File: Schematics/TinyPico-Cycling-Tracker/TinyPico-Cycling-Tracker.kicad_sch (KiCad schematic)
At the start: 7 parts, among them SW1 SW_Push, U1 TinyPico, U2 module_mpu6050, U3 SSD1306 0.96" OLED, U4 GPS6MV2, U5 MicroSD Card Adapter

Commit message: fix: use 5V power pin only
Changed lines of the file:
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@@
-	)
-	(junction
-		(at 113.03 35.56)
-		(diameter 0)
-		(color 0 0 0 0)
 	)
 	(junction
@@
 	(wire
 		(pts
-			(xy 113.03 35.56) (xy 143.51 35.56)
+			(xy 91.44 35.56) (xy 143.51 35.56)
 		)
 		(stroke
@@
 	(wire
 		(pts
-			(xy 113.03 33.02) (xy 113.03 35.56)
-		)
-		(stroke
-			(width 0)
-			(type default)
-		)
-	)
-	(wire
-		(pts
 			(xy 110.49 57.15) (xy 120.65 57.15)
 		)
@@
 		(pts
 			(xy 147.32 43.18) (xy 168.91 43.18)
-		)
-		(stroke
-			(width 0)
-			(type default)
-		)
-	)
-	(wire
-		(pts
-			(xy 91.44 35.56) (xy 113.03 35.56)
 		)
 		(stroke
@@
 					(unit 1)
 				)
-			)
-		)
-	)
-	(symbol
-		(lib_id "power:PWR_FLAG")
-		(at 113.03 33.02 0)
-		(unit 1)
-		(exclude_from_sim no)
-		(in_bom yes)
-		(on_board yes)
-		(dnp no)
-		(fields_autoplaced yes)
-		(property "Reference" "#FLG01"
-			(at 113.03 31.115 0)
-			(effects
-				(font
-					(size 1.27 1.27)
-				)
-				(hide yes)
-			)
-		)
-		(property "Value" "PWR_FLAG"
-			(at 113.03 27.94 0)
-			(effects
-				(font
-					(size 1.27 1.27)
-				)
-			)
-		)
-		(property "Footprint" ""
-			(at 113.03 33.02 0)
-			(effects
-				(font
-					(size 1.27 1.27)
-				)
-				(hide yes)
-			)
-		)
-		(property "Datasheet" "~"
-			(at 113.03 33.02 0)
-			(effects
-				(font
-					(size 1.27 1.27)
-				)
-				(hide yes)
-			)
-		)
-		(property "Description" "Special symbol for telling ERC where power comes from"
-			(at 113.03 33.02 0)
-			(effects
-				(font
-					(size 1.27 1.27)
-				)
-				(hide yes)
-			)
-		)
-		(pin "1"
-		)
-		(instances
-			(project ""
-				(path "/c19b4b11-d562-4619-8198-7fbe4f513d32"
-					(reference "#FLG01")
-					(unit 1)
-				)

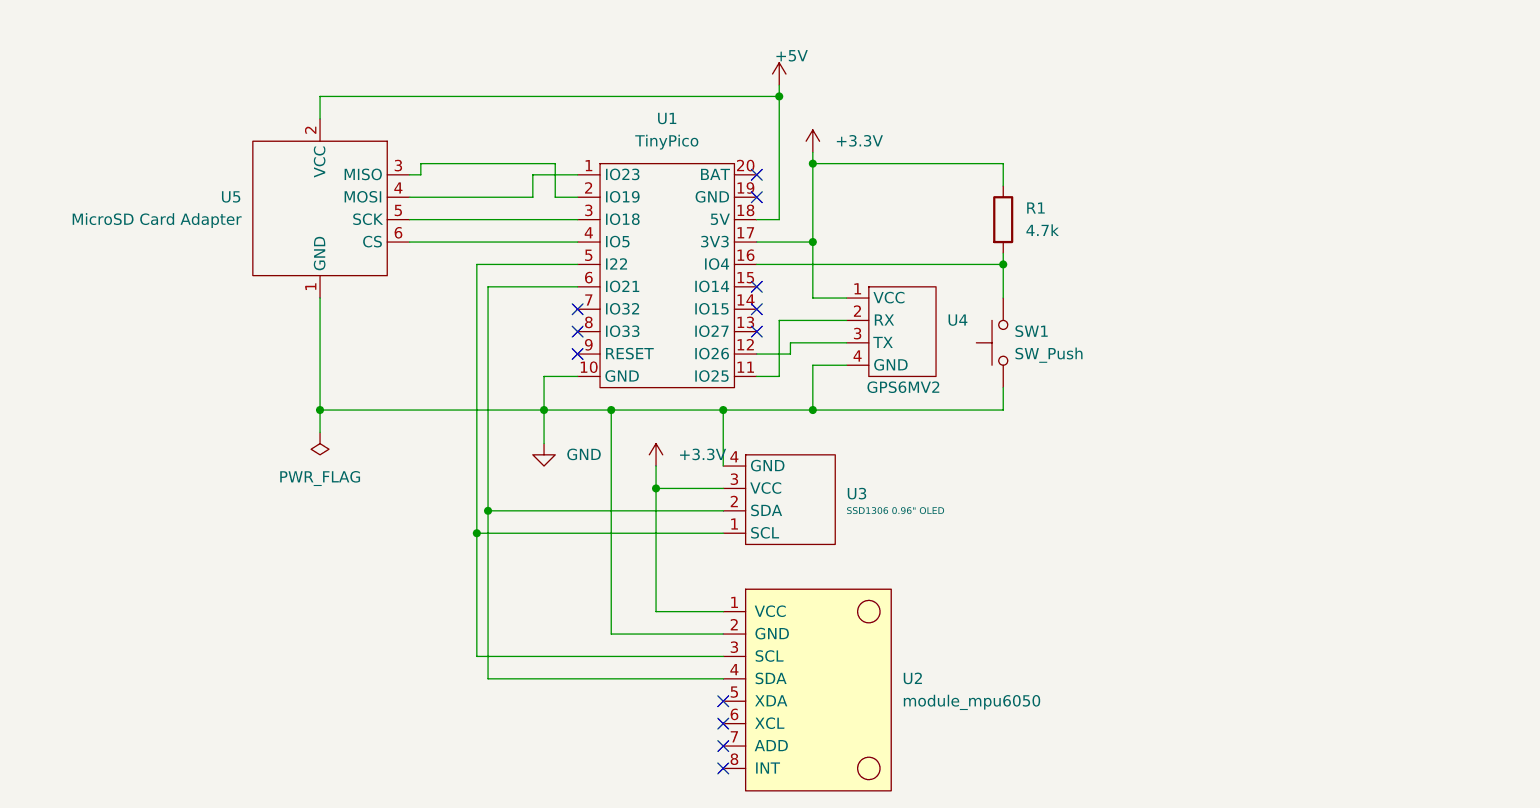
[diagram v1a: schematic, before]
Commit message: chore: use multisheet for the schematic
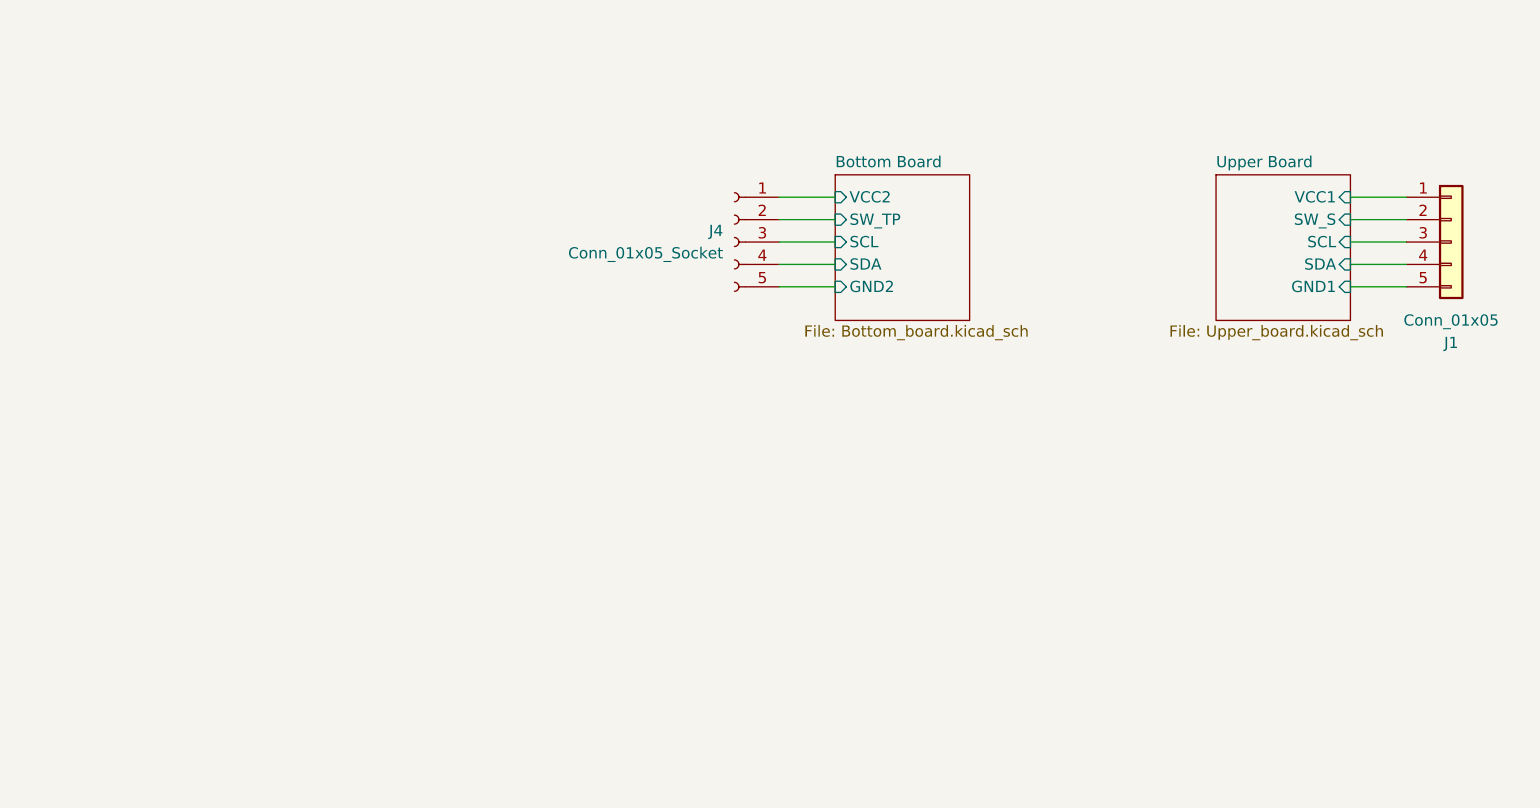
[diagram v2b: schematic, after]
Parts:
- removed R1: 4.7k, symbol Device:R
- removed SW1: SW_Push, symbol Switch:SW_Push
- removed U1: TinyPico, symbol TinyPico:TinyPICO_V2_USBC
- removed U2: module_mpu6050, usini_kicad_sensors:module_mpu6050, symbol usini_kicad_sensors:module_mpu6050
- removed U3: SSD1306 0.96" OLED, symbol Soldered:SSD1306-0.96{dblquote}-I2C-OLED-Display
- removed U4: GPS6MV2, symbol uBlox-NEO-6M:_GPS6MV2
- removed U5: MicroSD Card Adapter, symbol MicroSD-Card-Adapter:_MicroSD-Card-Adapter
- added J1: Conn_01x05, Connector_PinHeader_2.54mm:PinHeader_1x05_P2.54mm_Vertical, symbol Connector_Generic:Conn_01x05
- added J4: Conn_01x05_Socket, Connector_PinSocket_2.54mm:PinSocket_1x05_P2.54mm_Vertical, symbol Connector:Conn_01x05_Socket
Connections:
- new net Bottom Board/GND2: J4.5 (Pin_5)
- new net Bottom Board/SCL: J4.3 (Pin_3)
- new net Bottom Board/SDA: J4.4 (Pin_4)
- new net Bottom Board/SW_TP: J4.2 (Pin_2)
- new net Bottom Board/VCC2: J4.1 (Pin_1)
- new net Upper Board/GND1: J1.5 (Pin_5)
- new net Upper Board/SCL: J1.3 (Pin_3)
- new net Upper Board/SDA: J1.4 (Pin_4)
- new net Upper Board/SW_S: J1.2 (Pin_2)
- new net Upper Board/VCC1: J1.1 (Pin_1)
- no-connect marks 12 -> 0
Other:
- added sheet Bottom Board (Bottom_board.kicad_sch)
- added sheet Upper Board (Upper_board.kicad_sch)

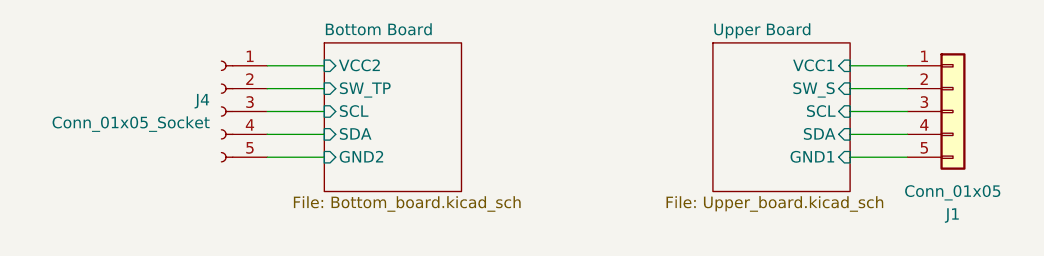
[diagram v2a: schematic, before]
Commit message: chore: INT in schematic and PCB
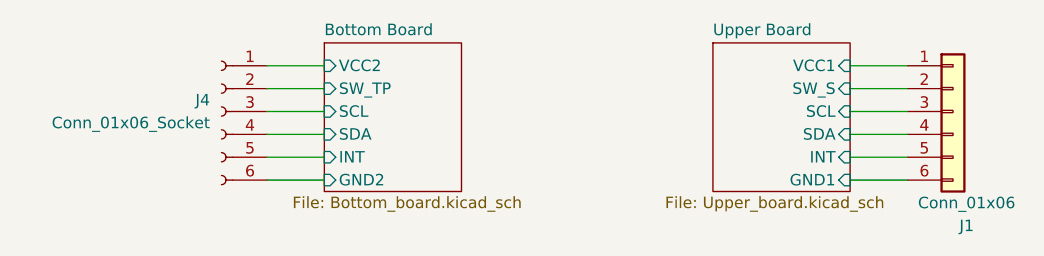
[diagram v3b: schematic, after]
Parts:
- J1: value Conn_01x05 -> Conn_01x06; footprint Connector_PinHeader_2.54mm:PinHeader_1x05_P2.54mm_Vertical -> Connector_PinHeader_2.54mm:PinHeader_1x06_P2.54mm_Vertical; symbol Connector_Generic:Conn_01x05 -> Connector_Generic:Conn_01x06
- J4: value Conn_01x05_Socket -> Conn_01x06_Socket; footprint Connector_PinSocket_2.54mm:PinSocket_1x05_P2.54mm_Vertical -> Connector_PinSocket_2.54mm:PinSocket_1x06_P2.54mm_Vertical; symbol Connector:Conn_01x05_Socket -> Connector:Conn_01x06_Socket
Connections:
- net Bottom Board/GND2: now also J4.6 (Pin_6); no longer J4.5 (Pin_5)
- net Upper Board/GND1: now also J1.6 (Pin_6); no longer J1.5 (Pin_5)
- new net Bottom Board/INT: J4.5 (Pin_5)
- new net Upper Board/INT: J1.5 (Pin_5)
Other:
- sheet Bottom Board ports: added INT; removed none
- sheet Upper Board ports: added INT; removed none
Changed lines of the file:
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@@
+	(wire
+		(pts
+			(xy 208.28 46.99) (xy 214.63 46.99)
+		)
+		(stroke
+			(width 0)
+			(type default)
+		)
+	)
+	(wire
+		(pts
+			(xy 208.28 57.15) (xy 214.63 57.15)
+		)
+		(stroke
+			(width 0)
+			(type default)
+		)
+	)
+	(wire
+		(pts
+			(xy 143.51 54.61) (xy 149.86 54.61)
+		)
+		(stroke
+			(width 0)
+			(type default)
+		)
+	)
+	(wire
+		(pts
+			(xy 143.51 49.53) (xy 149.86 49.53)
+		)
+		(stroke
+			(width 0)
+			(type default)
+		)
+	)
+	(wire
+		(pts
+			(xy 208.28 59.69) (xy 214.63 59.69)
+		)
+		(stroke
+			(width 0)
+			(type default)
+		)
+	)
+	(wire
+		(pts
+			(xy 208.28 49.53) (xy 214.63 49.53)
+		)
+		(stroke
+			(width 0)
+			(type default)
+		)
+	)
+	(wire
+		(pts
+			(xy 143.51 46.99) (xy 149.86 46.99)
+		)
+		(stroke
+			(width 0)
+			(type default)
+		)
+	)
 	(wire
 		(pts
@@
 	(wire
 		(pts
-			(xy 208.28 46.99) (xy 214.63 46.99)
-		)
-		(stroke
-			(width 0)
-			(type default)
-		)
-	)
-	(wire
-		(pts
-			(xy 143.51 54.61) (xy 149.86 54.61)
-		)
-		(stroke
-			(width 0)
-			(type default)
-		)
-	)
-	(wire
-		(pts
-			(xy 143.51 49.53) (xy 149.86 49.53)
-		)
-		(stroke
-			(width 0)
-			(type default)
-		)
-	)
-	(wire
-		(pts
-			(xy 208.28 49.53) (xy 214.63 49.53)
-		)
-		(stroke
-			(width 0)
-			(type default)
-		)
-	)
-	(wire
-		(pts
-			(xy 208.28 57.15) (xy 214.63 57.15)
-		)
-		(stroke
-			(width 0)
-			(type default)
-		)
-	)
-	(wire
-		(pts
-			(xy 143.51 46.99) (xy 149.86 46.99)
-		)
-		(stroke
-			(width 0)
-			(type default)
-		)
-	)
-	(wire
-		(pts
 			(xy 208.28 52.07) (xy 214.63 52.07)
 		)
@@
 	(wire
 		(pts
+			(xy 143.51 59.69) (xy 149.86 59.69)
+		)
+		(stroke
+			(width 0)
+			(type default)
+		)
+	)
+	(wire
+		(pts
 			(xy 208.28 54.61) (xy 214.63 54.61)
 		)
@@
 	)
 	(symbol
-		(lib_id "Connector:Conn_01x05_Socket")
+		(lib_id "Connector:Conn_01x06_Socket")
 		(at 138.43 52.07 0)
 		(mirror y)
@@
 			)
 		)
-		(property "Value" "Conn_01x05_Socket"
+		(property "Value" "Conn_01x06_Socket"
 			(at 137.16 53.3399 0)
 			(effects
@@
 			)
 		)
-		(property "Footprint" "Connector_PinSocket_2.54mm:PinSocket_1x05_P2.54mm_Vertical"
+		(property "Footprint" "Connector_PinSocket_2.54mm:PinSocket_1x06_P2.54mm_Vertical"
 			(at 138.43 52.07 0)
 			(effects
@@
 			)
 		)
-		(property "Description" "Generic connector, single row, 01x05, script generated"
+		(property "Description" "Generic connector, single row, 01x06, script generated"
 			(at 138.43 52.07 0)
 			(effects
@@
 		(pin "5"
 		)
+		(pin "6"
+		)
 		(instances
-			(project ""
+			(project "TinyPico-Cycling-Tracker"
 				(path "/c19b4b11-d562-4619-8198-7fbe4f513d32"
 					(reference "J4")
@@
 	)
 	(symbol
-		(lib_id "Connector_Generic:Conn_01x05")
+		(lib_id "Connector_Generic:Conn_01x06")
 		(at 219.71 52.07 0)
 		(unit 1)
@@
 		(dnp no)
 		(property "Reference" "J1"
-			(at 219.71 63.5 0)
-			(effects
-				(font
-					(size 1.27 1.27)
-				)
-			)
-		)
-		(property "Value" "Conn_01x05"
-			(at 219.71 60.96 0)
-			(effects
-				(font
-					(size 1.27 1.27)
-				)
-			)
-		)
-		(property "Footprint" "Connector_PinHeader_2.54mm:PinHeader_1x05_P2.54mm_Vertical"
+			(at 221.234 64.77 0)
+			(effects
+				(font
+					(size 1.27 1.27)
+				)
+			)
+		)
+		(property "Value" "Conn_01x06"
+			(at 221.234 62.23 0)
+			(effects
+				(font
+					(size 1.27 1.27)
+				)
+			)
+		)
+		(property "Footprint" "Connector_PinHeader_2.54mm:PinHeader_1x06_P2.54mm_Vertical"
 			(at 219.71 52.07 0)
 			(effects
@@
 			)
 		)
-		(property "Description" "Generic connector, single row, 01x05, script generated (kicad-library-utils/schlib/autogen/connector/)"
+		(property "Description" "Generic connector, single row, 01x06, script generated (kicad-library-utils/schlib/autogen/connector/)"
 			(at 219.71 52.07 0)
 			(effects
@@
 		(pin "1"
 		)
+		(pin "6"
+		)
 		(instances
-			(project ""
+			(project "TinyPico-Cycling-Tracker"
 				(path "/c19b4b11-d562-4619-8198-7fbe4f513d32"
 					(reference "J1")
@@
 		)
 		(pin "GND1" input
-			(at 208.28 57.15 0)
+			(at 208.28 59.69 0)
 			(effects
 				(font
@@
 		(pin "VCC1" input
 			(at 208.28 46.99 0)
+			(effects
+				(font
+					(size 1.27 1.27)
+				)
+				(justify right)
+			)
+		)
+		(pin "INT" input
+			(at 208.28 57.15 0)
 			(effects
 				(font
@@
 		)
 		(pin "GND2" input
-			(at 149.86 57.15 180)
+			(at 149.86 59.69 180)
 			(effects
 				(font
@@
 			(effects
 				(font
+					(size 1.27 1.27)
+				)
+				(justify left)
+			)
+		)
+		(pin "INT" input
+			(at 149.86 57.15 180)
+			(effects
+				(font
